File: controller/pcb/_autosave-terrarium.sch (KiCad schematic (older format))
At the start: 59 parts, among them K1 G3MB-202P, K2 G3MB-202P, K3 G3MB-202P, Q1 S8050, Q2 S8050, Q3 S8050, SW1 RST, U1 ESP32-WROOM-32, U2 DS3231M, U5 TCA9548APWR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

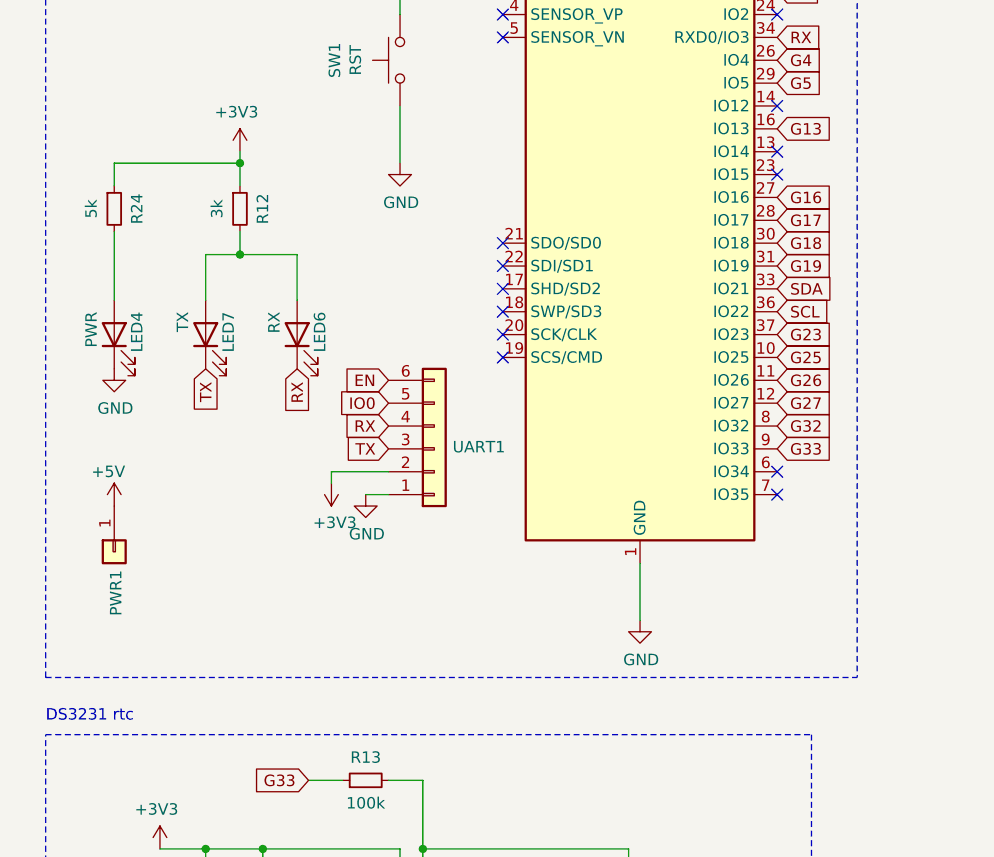
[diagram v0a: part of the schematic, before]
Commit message: Controller pcb/v1.7 (#5)
* move components around

* pcb v1.7 done

Co-authored-by: Grigorii Merkushev <brushknight@pop-os.localdomain>
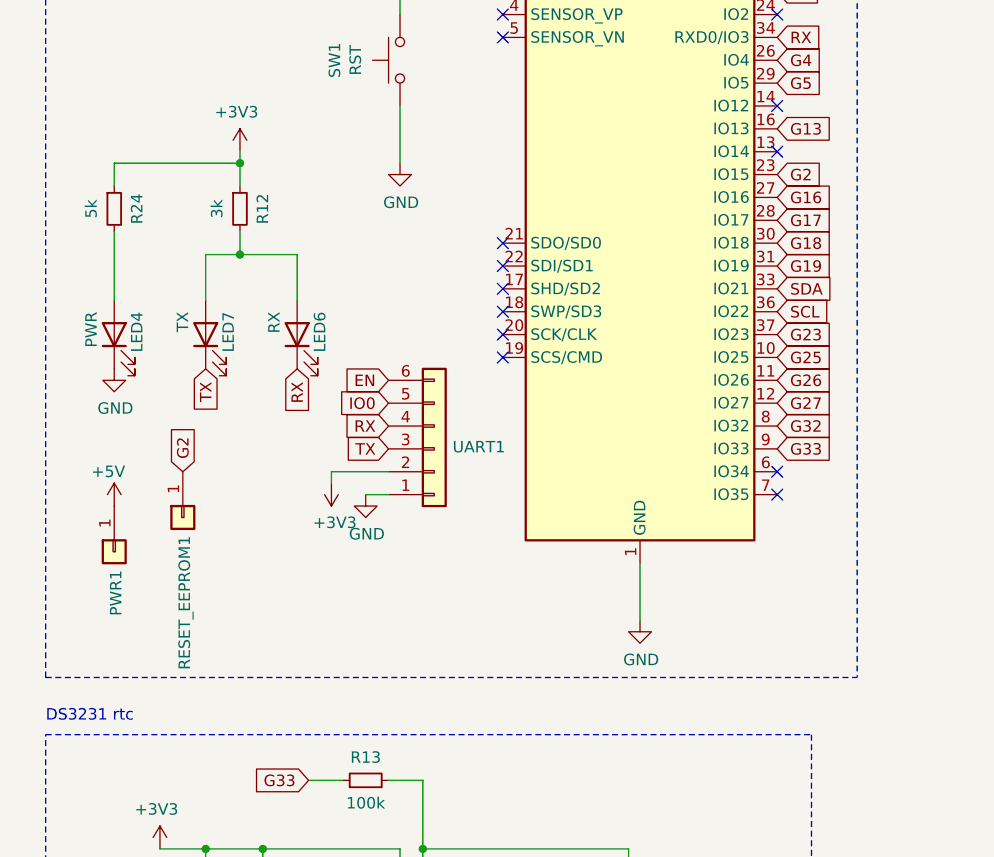
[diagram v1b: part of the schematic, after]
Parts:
- added RESET_EEPROM1: data, Connector_PinHeader_2.54mm:PinHeader_1x01_P2.54mm_Vertical, symbol Connector_Generic:Conn_01x01
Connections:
- net G2: now reaches U1.23 (IO15)
- net G2: now also RESET_EEPROM1.1 (Pin_1)
- no-connect marks 18 -> 17
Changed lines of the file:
@@
 NoConn ~ 10050 2200
 NoConn ~ 10050 2400
-NoConn ~ 10050 2500
 NoConn ~ 10050 3800
 NoConn ~ 10050 3900
@@
 Wire Wire Line
 	1700 6000 1600 6000
+$Comp
+L Connector_Generic:Conn_01x01 RESET_EEPROM1
+U 1 1 62BA3F8C
+P 7450 4000
+F 0 "RESET_EEPROM1" H 7530 3992 50  0000 L CNN
+F 1 "data" H 7600 3400 50  0001 L CNN
+F 2 "Connector_PinHeader_2.54mm:PinHeader_1x01_P2.54mm_Vertical" H 7450 4000 50  0001 C CNN
+F 3 "~" H 7450 4000 50  0001 C CNN
+	1    7450 4000
+	0    -1   1    0
+$EndComp
+Text GLabel 7450 3800 1    50   Input ~ 0
+G2
+Text GLabel 10050 2500 2    50   Input ~ 0
+G2
 $EndSCHEMATC
